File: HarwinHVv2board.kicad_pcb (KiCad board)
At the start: 2 copper layers, 12 x 26 mm, 7 parts, among them J1 HV2, J2 GND2, J3 HarwinHV1, J4 HarwinHV2, J5 HarwinGND, J6 HV1, J7 GND1

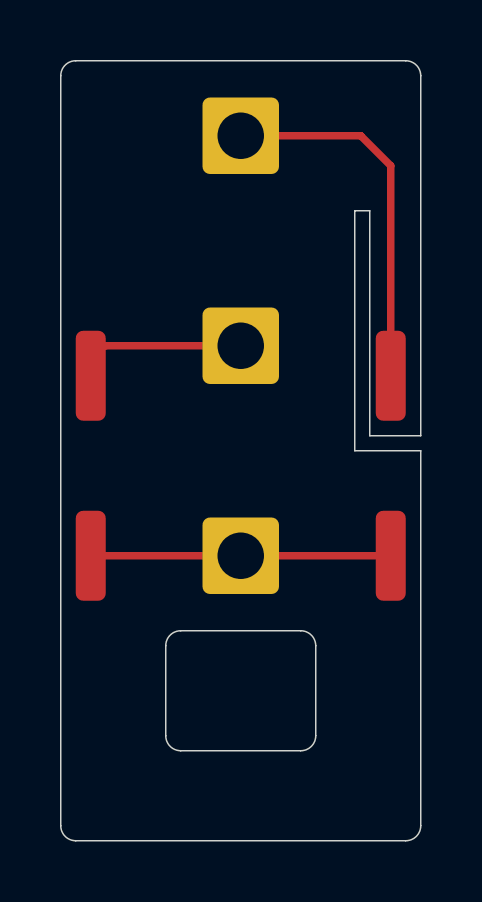
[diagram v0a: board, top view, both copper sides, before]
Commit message: Changed Harwin connector pads to 1.3mm drill hole on a 5.75 x 2 mm rectangular pad with rounded corners.
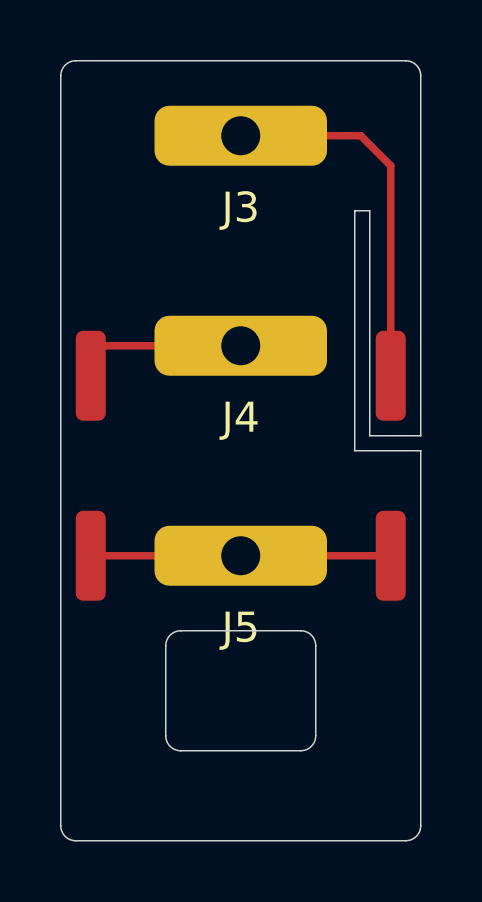
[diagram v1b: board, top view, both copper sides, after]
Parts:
- J3, J4, J5: footprint Connector_Wire:SolderWire-0.75sqmm_1x01_D1.25mm_OD2.3mm -> HarwinHVv2board:Pin_D1.3mm_L5.75mmW2.0mm
